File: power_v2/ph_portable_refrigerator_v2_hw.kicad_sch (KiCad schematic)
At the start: 0 parts

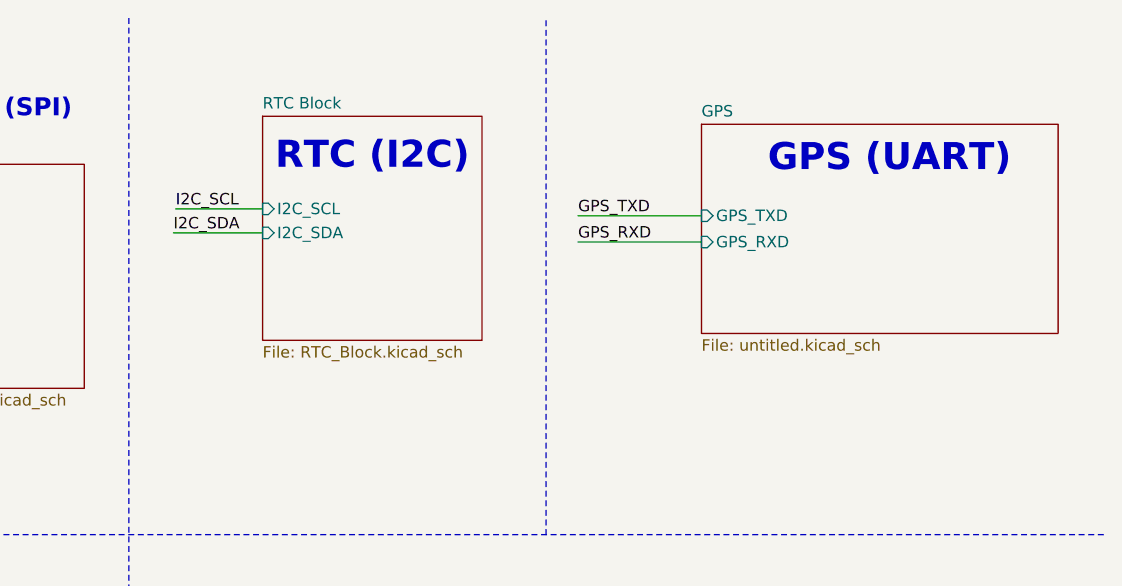
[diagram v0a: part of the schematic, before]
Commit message: Oder PCB, Viet tai lieu mo ta hardware
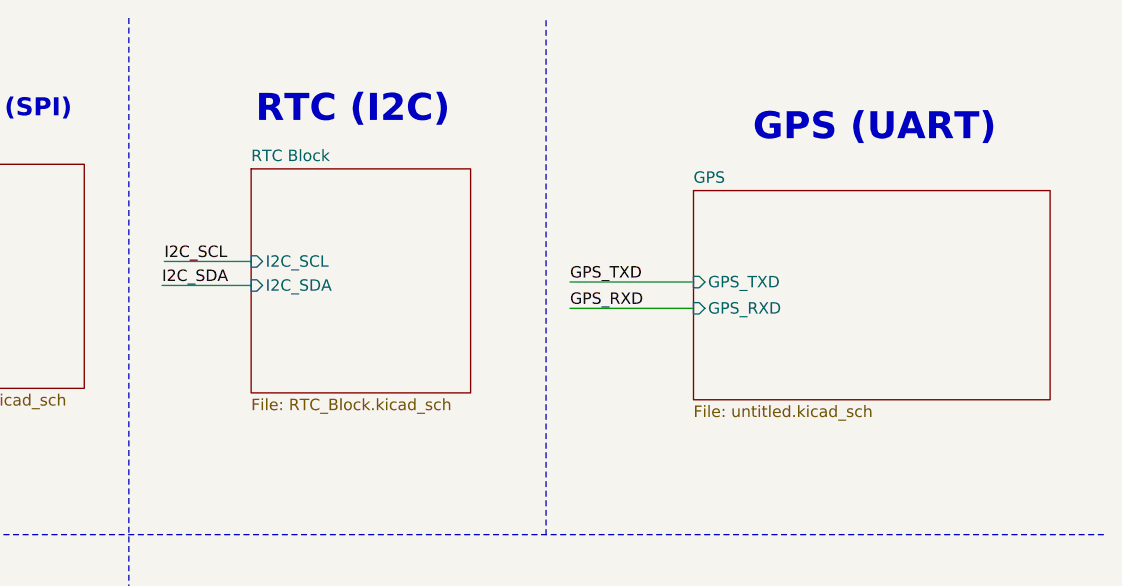
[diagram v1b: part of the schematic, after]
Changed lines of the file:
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@@
 (kicad_sch (version 20230121) (generator eeschema)
   (paper "A4")
-  (wire (pts (xy 181.737 35.56) (xy 191.643 35.56))
+  (wire (pts (xy 180.467 41.402) (xy 190.373 41.402))
     (stroke (width 0) (type default))
   )
@@
     (stroke (width 0) (type default))
   )
-  (wire (pts (xy 226.695 36.576) (xy 240.411 36.576))
+  (wire (pts (xy 225.806 43.942) (xy 239.522 43.942))
     (stroke (width 0) (type default))
   )
@@
     (stroke (width 0) (type default))
   )
-  (wire (pts (xy 191.643 32.893) (xy 181.991 32.893))
+  (wire (pts (xy 190.373 38.735) (xy 180.721 38.735))
     (stroke (width 0) (type default))
   )
@@
     (stroke (width 0) (type default))
   )
-  (wire (pts (xy 226.695 33.655) (xy 240.411 33.655))
+  (wire (pts (xy 225.806 41.021) (xy 239.522 41.021))
     (stroke (width 0) (type default))
   )
@@
     (effects (font (size 2 2) (thickness 0.6) bold) (justify left bottom))
   )
-  (text "GPS (UART)" (at 247.777 29.083 0)
+  (text "GPS (UART)" (at 246.126 25.654 0)
     (effects (font (size 3 3) (thickness 1) bold) (justify left bottom))
   )
@@
     (effects (font (size 3 3) (thickness 0.6) bold) (justify left bottom))
   )
-  (text "RTC (I2C)" (at 193.04 28.829 0)
+  (text "RTC (I2C)" (at 190.881 23.622 0)
     (effects (font (size 3 3) (thickness 0.6) bold) (justify left bottom))
   )
@@
     (effects (font (size 1.27 1.27)) (justify left bottom))
   )
-  (label "I2C_SCL" (at 181.991 32.893 0) (fields_autoplaced)
+  (label "I2C_SCL" (at 180.721 38.735 0) (fields_autoplaced)
     (effects (font (size 1.27 1.27)) (justify left bottom))
   )
@@
     (effects (font (size 1.27 1.27)) (justify right bottom))
   )
-  (label "I2C_SDA" (at 181.737 35.56 0) (fields_autoplaced)
+  (label "I2C_SDA" (at 180.467 41.402 0) (fields_autoplaced)
     (effects (font (size 1.27 1.27)) (justify left bottom))
   )
@@
     (effects (font (size 1.27 1.27)) (justify left bottom))
   )
-  (label "GPS_TXD" (at 226.695 33.655 0) (fields_autoplaced)
+  (label "GPS_TXD" (at 225.806 41.021 0) (fields_autoplaced)
     (effects (font (size 1.27 1.27)) (justify left bottom))
   )
@@
     (effects (font (size 1.27 1.27)) (justify right bottom))
   )
-  (label "GPS_RXD" (at 226.695 36.576 0) (fields_autoplaced)
+  (label "GPS_RXD" (at 225.806 43.942 0) (fields_autoplaced)
     (effects (font (size 1.27 1.27)) (justify left bottom))
   )
@@
     )
   )
-  (sheet (at 240.411 23.495) (size 39.624 23.241) (fields_autoplaced)
+  (sheet (at 239.522 30.861) (size 39.624 23.241) (fields_autoplaced)
     (stroke (width 0.1524) (type solid))
     (fill (color 0 0 0 0.0000))
-    (property "Sheetname" "GPS" (at 240.411 22.7834 0)
+    (property "Sheetname" "GPS" (at 239.522 30.1494 0)
       (effects (font (size 1.27 1.27)) (justify left bottom))
     )
-    (property "Sheetfile" "untitled.kicad_sch" (at 240.411 47.3206 0)
+    (property "Sheetfile" "untitled.kicad_sch" (at 239.522 54.6866 0)
       (effects (font (size 1.27 1.27)) (justify left top))
     )
-    (pin "GPS_TXD" input (at 240.411 33.655 180)
-      (effects (font (size 1.27 1.27)) (justify left))
-    )
-    (pin "GPS_RXD" input (at 240.411 36.576 180)
+    (pin "GPS_TXD" input (at 239.522 41.021 180)
+      (effects (font (size 1.27 1.27)) (justify left))
+    )
+    (pin "GPS_RXD" input (at 239.522 43.942 180)
       (effects (font (size 1.27 1.27)) (justify left))
     )
@@
     )
   )
-  (sheet (at 191.643 22.606) (size 24.384 24.892) (fields_autoplaced)
+  (sheet (at 190.373 28.448) (size 24.384 24.892) (fields_autoplaced)
     (stroke (width 0.1524) (type solid))
     (fill (color 0 0 0 0.0000))
-    (property "Sheetname" "RTC Block" (at 191.643 21.8944 0)
+    (property "Sheetname" "RTC Block" (at 190.373 27.7364 0)
       (effects (font (size 1.27 1.27)) (justify left bottom))
     )
-    (property "Sheetfile" "RTC_Block.kicad_sch" (at 191.643 48.0826 0)
+    (property "Sheetfile" "RTC_Block.kicad_sch" (at 190.373 53.9246 0)
       (effects (font (size 1.27 1.27)) (justify left top))
     )
-    (property "Field2" "" (at 191.643 22.606 0)
+    (property "Field2" "" (at 190.373 28.448 0)
       (effects (font (size 1.27 1.27)) hide)
     )
-    (pin "I2C_SCL" input (at 191.643 32.893 180)
-      (effects (font (size 1.27 1.27)) (justify left))
-    )
-    (pin "I2C_SDA" input (at 191.643 35.56 180)
-      (effects (font (size 1.27 1.27)) (justify left))
-    )
+    (pin "I2C_SCL" input (at 190.373 38.735 180)
+      (effects (font (size 1.27 1.27)) (justify left))
+    )
+    (pin "I2C_SDA" input (at 190.373 41.402 180)
+      (effects (font (size 1.27 1.27)) (justify left))
+    )
